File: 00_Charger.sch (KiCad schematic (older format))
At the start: 27 parts

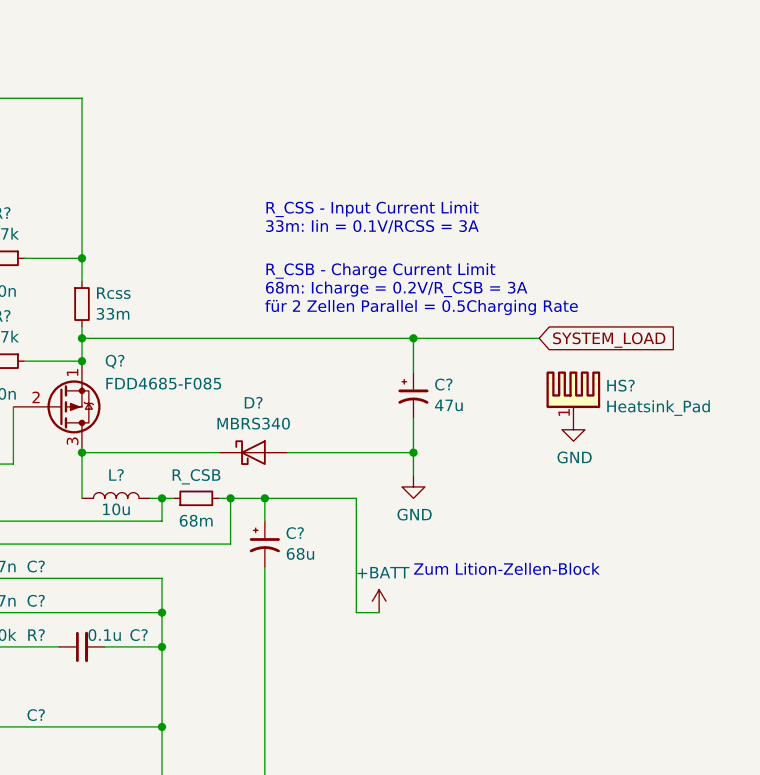
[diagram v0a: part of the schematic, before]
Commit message: BMS fertig, Charger fertig, Amplifier fertig. TODO: Charge vs Discharge LiPo wie machen sachen
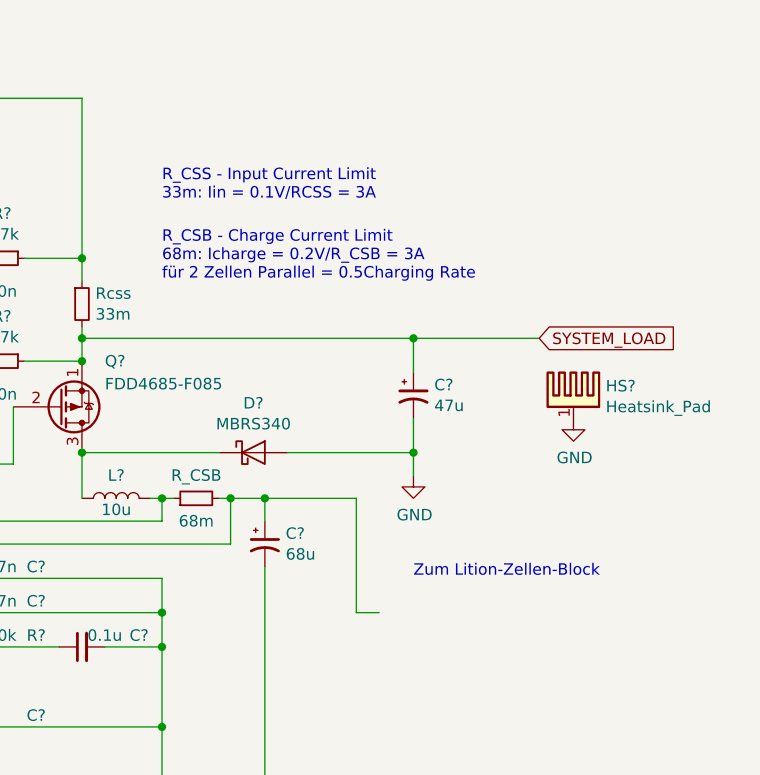
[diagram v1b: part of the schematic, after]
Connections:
- net labels removed: +BATT
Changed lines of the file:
@@
-$EndComp
-$Comp
-L Device:CP1_Small C?
-U 1 1 5E75D16E
-P 8050 3400
-F 0 "C?" H 8141 3446 50  0000 L CNN
-F 1 "47u" H 8141 3355 50  0000 L CNN
-F 2 "" H 8050 3400 50  0001 C CNN
-F 3 "~" H 8050 3400 50  0001 C CNN
-	1    8050 3400
-	1    0    0    -1
 $EndComp
 $Comp
@@
 Connection ~ 6600 2800
 Wire Wire Line
-	6600 3100 6600 3150
-Wire Wire Line
 	6600 3250 6350 3250
 Wire Wire Line
@@
 	7400 3850 7400 3950
 Connection ~ 7250 3850
-Wire Wire Line
-	7400 3850 7800 3850
-Wire Wire Line
-	7800 3850 7800 4350
 Connection ~ 7400 3850
 $Comp
@@
 	1    0    0    -1
 $EndComp
-Wire Wire Line
-	8050 3150 8050 3300
 $Comp
 L Device:D_Schottky D?
@@
 Wire Wire Line
 	6600 3650 7200 3650
-Wire Wire Line
-	6600 3150 8050 3150
-Connection ~ 6600 3150
-Wire Wire Line
-	6600 3150 6600 3250
 Connection ~ 6600 3250
 Wire Wire Line
@@
 Wire Wire Line
 	6950 3850 6950 3950
-Wire Wire Line
-	8050 3500 8050 3650
-Wire Wire Line
-	7500 3650 8050 3650
-Connection ~ 8050 3650
-Wire Wire Line
-	8050 3650 8050 3750
-Text GLabel 8600 3150 2    50   Input ~ 0
-SYSTEM_LOAD
-Wire Wire Line
-	8600 3150 8050 3150
-Connection ~ 8050 3150
 $Comp
 L Device:Q_NMOS_DGS Q?
@@
 Wire Wire Line
 	2700 3850 2950 3850
-Text Notes 7400 3050 0    50   ~ 0
+Text Notes 6950 2900 0    50   ~ 0
 R_CSB - Charge Current Limit\n68m: Icharge = 0.2V/R_CSB = 3A\nfür 2 Zellen Parallel = 0.5Charging Rate\n
 Text Notes 4000 5600 0    50   ~ 0
@@
 Text Notes 4900 1650 0    50   ~ 0
 T Version des IC für 4 Li-Ion Zellen
-$Comp
-L power:+BATT #PWR?
-U 1 1 5E811BF9
-P 7900 4350
-F 0 "#PWR?" H 7900 4200 50  0001 C CNN
-F 1 "+BATT" H 7915 4523 50  0000 C CNN
-F 2 "" H 7900 4350 50  0001 C CNN
-F 3 "" H 7900 4350 50  0001 C CNN
-	1    7900 4350
-	1    0    0    -1
-$EndComp
-Wire Wire Line
-	7900 4350 7800 4350
-Text Notes 7400 2700 0    50   ~ 0
+Text Notes 6950 2550 0    50   ~ 0
 R_CSS - Input Current Limit\n33m: Iin = 0.1V/RCSS = 3A
 $Comp
@@
 	1    0    0    -1
 $EndComp
+Wire Wire Line
+	7400 3850 7800 3850
+Wire Wire Line
+	7800 3850 7800 4350
+Wire Wire Line
+	7900 4350 7800 4350
+Wire Wire Line
+	8050 3650 8050 3750
+Wire Wire Line
+	7500 3650 8050 3650
+Connection ~ 8050 3650
+Wire Wire Line
+	8050 3500 8050 3650
+Wire Wire Line
+	8050 3150 8050 3300
+Wire Wire Line
+	8600 3150 8050 3150
+Connection ~ 8050 3150
+Wire Wire Line
+	6600 3150 6600 3250
+Wire Wire Line
+	6600 3100 6600 3150
+Connection ~ 6600 3150
+Wire Wire Line
+	6600 3150 8050 3150
+$Comp
+L Device:CP1_Small C?
+U 1 1 5E75D16E
+P 8050 3400
+F 0 "C?" H 8141 3446 50  0000 L CNN
+F 1 "47u" H 8141 3355 50  0000 L CNN
+F 2 "" H 8050 3400 50  0001 C CNN
+F 3 "~" H 8050 3400 50  0001 C CNN
+	1    8050 3400
+	1    0    0    -1
+$EndComp
+Text GLabel 8600 3150 2    50   Input ~ 0
+SYSTEM_LOAD
 $EndSCHEMATC

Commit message: 3v3 über LDO von BMS enablen. Bluetooth hinzugefügt
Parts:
- added J401: Jack-DC, symbol Connector:Jack-DC
- gave numbers to parts that had none: 25
- renumbered R_CSB to R_CSB401, Rcss to Rcss401
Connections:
- net labels added: DC_20V_POWER_SUPPLY, GNDPWR, PACK+
- net labels removed: VCC
- wire segments 81 -> 82
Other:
- note added: "GND über Shunt verbinden"
- note added: "Spannung 20V in Ladekabel"

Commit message: Schaltplan fertig. Fertig für review
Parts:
- removed Q401: NMOS, symbol Device:Q_NMOS_DGS
- added C?: 1000uF, symbol Device:C_Small
- added L?: 25mH, symbol Device:L_Small
- added Q?: NTK3043N, symbol Device:Q_NMOS_GSD
- added R?: 10k, symbol Device:R_Small
- added R?: 100K, symbol Device:R_Small
- added R? (x7): 1K, symbol Device:R_Small
- added R?: 10K, symbol Device:R_Small
- added R?: 1M, symbol Device:R_Small
- added U?: PC827, Package_DIP:DIP-8_W7.62mm, symbol Isolator:PC827
- L401: value 10u -> 10uH
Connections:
- net CHARGER_DISABLE: now also R?.1
- net CHARGER_IOUT: now also R?.1, R?.2; no longer U401.7 (IOUT)
- net DC_20V_POWER_SUPPLY: now also R?.1, R?.2
- net GND: now also Q?.2 (S), R?.1, R?.1, R?.2, U?.2, U?.7
- net GNDPWR: now also C?.2
- net at C402.1, C403.2, R405.1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: now also C?.1, L?.2; no longer D401.1 (K)
- net at R401.2, U401.6 (ICHG/EN): now also Q?.3 (D)
- new net: D401.1 (K), L?.1
- new net: Q?.1 (G), R?.1, R?.2
- new net: R?.2, U?.1
- new net: R?.1, R?.2 (x4)
- new net +3V3: R?.1
- new net CHARGER_PLUGGED: R?.2, U?.8
- new net IOUT: R?.2, U401.7 (IOUT)
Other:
- note added: "3,06V @ 3A Chargecurrent"
- note added: "4,08V @ 3A Chargecurrent"
- note added: "I=1mA"
- note added: "IOUT=20(R_SCB*I_CHG) = \n20*0,068*3A= 4,08V"
- note added: "LC-Tiefpass\n32Hz Grenzfrequenz"
- moved on the sheet: C401, C402, C403, C404, C405, C406, C407, C408, C409, C410, C411, C412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

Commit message: Footprintzuordnung angefangen
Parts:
- C401, C402, C403, C404, C405, C406, C407, C408, C409, C410: footprint (none) -> Capacitor_SMD:C_0603_1608Metric_Pad1.05x0.95mm_HandSolder
- C411, C412: footprint (none) -> Capacitor_SMD:CP_Elec_5x5.4
- C413: renamed from C?; footprint (none) -> Capacitor_SMD:CP_Elec_16x17.5
- gave numbers to parts that had none: 14
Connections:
- net POWER_SUPPLY: now reaches C402.1, C403.2, C413.1, L402.2, R405.1, Rcss401.1, U401.15 (DCIN)
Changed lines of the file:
@@
 F 0 "C408" V 7400 4100 50  0000 C CNN
 F 1 "47n" V 7400 4300 50  0000 C CNN
-F 2 "" H 7350 4450 50  0001 C CNN
+F 2 "Capacitor_SMD:C_0603_1608Metric_Pad1.05x0.95mm_HandSolder" H 7350 4450 50  0001 C CNN
 F 3 "~" H 7350 4450 50  0001 C CNN
 	1    7350 4450
@@
 F 0 "C401" H 4958 4004 50  0000 R CNN
 F 1 "1u" H 4958 4095 50  0000 R CNN
-F 2 "" H 5050 4050 50  0001 C CNN
+F 2 "Capacitor_SMD:C_0603_1608Metric_Pad1.05x0.95mm_HandSolder" H 5050 4050 50  0001 C CNN
 F 3 "~" H 5050 4050 50  0001 C CNN
 	1    5050 4050
@@
 F 0 "C409" V 7400 4650 50  0000 C CNN
 F 1 "1n" V 7400 4850 50  0000 C CNN
-F 2 "" H 7350 4950 50  0001 C CNN
+F 2 "Capacitor_SMD:C_0603_1608Metric_Pad1.05x0.95mm_HandSolder" H 7350 4950 50  0001 C CNN
 F 3 "~" H 7350 4950 50  0001 C CNN
 	1    7350 4950
@@
 F 0 "C402" V 5221 3100 50  0000 C CNN
 F 1 "220n" V 5312 3100 50  0000 C CNN
-F 2 "" H 5450 3100 50  0001 C CNN
+F 2 "Capacitor_SMD:C_0603_1608Metric_Pad1.05x0.95mm_HandSolder" H 5450 3100 50  0001 C CNN
 F 3 "~" H 5450 3100 50  0001 C CNN
 	1    5450 3100
@@
 F 0 "C407" V 7400 3950 50  0000 C CNN
 F 1 "47n" V 7400 4150 50  0000 C CNN
-F 2 "" H 7350 4300 50  0001 C CNN
+F 2 "Capacitor_SMD:C_0603_1608Metric_Pad1.05x0.95mm_HandSolder" H 7350 4300 50  0001 C CNN
 F 3 "~" H 7350 4300 50  0001 C CNN
 	1    7350 4300
@@
 F 0 "C410" V 7950 4350 50  0000 C CNN
 F 1 "0.1u" V 7900 4500 50  0000 C CNN
-F 2 "" H 7850 4600 50  0001 C CNN
+F 2 "Capacitor_SMD:C_0603_1608Metric_Pad1.05x0.95mm_HandSolder" H 7850 4600 50  0001 C CNN
 F 3 "~" H 7850 4600 50  0001 C CNN
 	1    7850 4600
@@
 F 0 "C403" V 5471 2900 50  0000 C CNN
 F 1 "220n" V 5562 2900 50  0000 C CNN
-F 2 "" H 5700 2900 50  0001 C CNN
+F 2 "Capacitor_SMD:C_0603_1608Metric_Pad1.05x0.95mm_HandSolder" H 5700 2900 50  0001 C CNN
 F 3 "~" H 5700 2900 50  0001 C CNN
 	1    5700 2900
@@
 F 0 "C404" V 6371 2450 50  0000 C CNN
 F 1 "2.2u" V 6462 2450 50  0000 C CNN
-F 2 "" H 6600 2450 50  0001 C CNN
+F 2 "Capacitor_SMD:C_0603_1608Metric_Pad1.05x0.95mm_HandSolder" H 6600 2450 50  0001 C CNN
 F 3 "~" H 6600 2450 50  0001 C CNN
 	1    6600 2450
@@
 F 0 "C405" H 7208 2954 50  0000 R CNN
 F 1 "220n" H 7208 3045 50  0000 R CNN
-F 2 "" H 7300 3000 50  0001 C CNN
+F 2 "Capacitor_SMD:C_0603_1608Metric_Pad1.05x0.95mm_HandSolder" H 7300 3000 50  0001 C CNN
 F 3 "~" H 7300 3000 50  0001 C CNN
 	1    7300 3000
@@
 F 0 "C406" H 7208 3404 50  0000 R CNN
 F 1 "220n" H 7208 3495 50  0000 R CNN
-F 2 "" H 7300 3450 50  0001 C CNN
+F 2 "Capacitor_SMD:C_0603_1608Metric_Pad1.05x0.95mm_HandSolder" H 7300 3450 50  0001 C CNN
 F 3 "~" H 7300 3450 50  0001 C CNN
 	1    7300 3450
@@
 	7850 2900 7600 2900
 Wire Wire Line
-	5550 2200 7850 2200
+	5550 2200 7450 2200
 Wire Wire Line
 	7850 2200 7850 2900
@@
 F 0 "C411" H 8741 4196 50  0000 L CNN
 F 1 "68u" H 8741 4105 50  0000 L CNN
-F 2 "" H 8650 4150 50  0001 C CNN
+F 2 "Capacitor_SMD:CP_Elec_5x5.4" H 8650 4150 50  0001 C CNN
 F 3 "~" H 8650 4150 50  0001 C CNN
 	1    8650 4150
@@
 	9300 3250 9300 3400
 Wire Wire Line
-	9850 3250 9300 3250
+	9850 3250 9600 3250
 Connection ~ 9300 3250
 Wire Wire Line
@@
 F 0 "C412" H 9391 3546 50  0000 L CNN
 F 1 "47u" H 9391 3455 50  0000 L CNN
-F 2 "" H 9300 3500 50  0001 C CNN
+F 2 "Capacitor_SMD:CP_Elec_5x5.4" H 9300 3500 50  0001 C CNN
 F 3 "~" H 9300 3500 50  0001 C CNN
 	1    9300 3500
@@
 DC_20V_POWER_SUPPLY
 $Comp
-L Device:Q_NMOS_GSD Q?
+L Device:Q_NMOS_GSD Q401
 U 1 1 5ECEE149
 P 4400 3950
-F 0 "Q?" H 4606 3996 50  0000 L CNN
+F 0 "Q401" H 4606 3996 50  0000 L CNN
 F 1 "NTK3043N" H 4606 3905 50  0000 L CNN
 F 2 "" H 4600 4050 50  0001 C CNN
@@
 $EndComp
 $Comp
-L Device:R_Small R?
+L Device:R_Small R415
 U 1 1 5ECEF6C1
 P 3850 3950
-F 0 "R?" V 3750 4000 50  0000 R CNN
+F 0 "R415" V 3750 4000 50  0000 R CNN
 F 1 "10k" V 3650 4000 50  0000 R CNN
 F 2 "" H 3850 3950 50  0001 C CNN
@@
 	3750 3950 3600 3950
 $Comp
-L Device:R_Small R?
+L Device:R_Small R417
 U 1 1 5EE5F4E2
 P 4100 4350
-F 0 "R?" H 4159 4396 50  0000 L CNN
+F 0 "R417" H 4159 4396 50  0000 L CNN
 F 1 "100K" H 4159 4305 50  0000 L CNN
 F 2 "" H 4100 4350 50  0001 C CNN
@@
 	4100 3950 4200 3950
 $Comp
-L power:GND #PWR?
+L power:GND #PWR0407
 U 1 1 5EE6150A
 P 4100 5200
-F 0 "#PWR?" H 4100 4950 50  0001 C CNN
+F 0 "#PWR0407" H 4100 4950 50  0001 C CNN
 F 1 "GND" H 4105 5027 50  0000 C CNN
 F 2 "" H 4100 5200 50  0001 C CNN
@@
 	4100 5200 4100 4450
 $Comp
-L Device:L_Small L?
+L Device:L_Small L402
 U 1 1 5EE6657B
 P 5000 2200
-F 0 "L?" V 5185 2200 50  0000 C CNN
+F 0 "L402" V 5185 2200 50  0000 C CNN
 F 1 "25mH" V 5094 2200 50  0000 C CNN
 F 2 "" H 5000 2200 50  0001 C CNN
@@
 Connection ~ 5550 2200
 $Comp
-L Device:C_Small C?
+L Device:C_Small C413
 U 1 1 5EE6A868
 P 5200 2400
-F 0 "C?" H 4850 2450 50  0000 L CNN
+F 0 "C413" H 4850 2450 50  0000 L CNN
 F 1 "1000uF" H 4850 2300 50  0000 L CNN
-F 2 "" H 5200 2400 50  0001 C CNN
+F 2 "Capacitor_SMD:CP_Elec_16x17.5" H 5200 2400 50  0001 C CNN
 F 3 "~" H 5200 2400 50  0001 C CNN
 	1    5200 2400
@@
 	5200 2200 5100 2200
 $Comp
-L power:GNDPWR #PWR?
+L power:GNDPWR #PWR0408
 U 1 1 5EE6CAF0
 P 5200 2500
-F 0 "#PWR?" H 5200 2300 50  0001 C CNN
+F 0 "#PWR0408" H 5200 2300 50  0001 C CNN
 F 1 "GNDPWR" H 5204 2346 50  0000 C CNN
 F 2 "" H 5200 2450 50  0001 C CNN
@@
 LC-Tiefpass\n32Hz Grenzfrequenz
 $Comp
-L Isolator:PC827 U?
+L Isolator:PC827 U402
 U 1 1 5EE6E88A
 P 3650 2900
-F 0 "U?" H 3650 3225 50  0000 C CNN
+F 0 "U402" H 3650 3225 50  0000 C CNN
 F 1 "PC827" H 3650 3134 50  0000 C CNN
 F 2 "Package_DIP:DIP-8_W7.62mm" H 3450 2700 50  0001 L CIN
@@
 	3350 2800 3150 2800
 $Comp
-L power:GND #PWR?
+L power:GND #PWR0404
 U 1 1 5EE80AA2
 P 3250 3100
-F 0 "#PWR?" H 3250 2850 50  0001 C CNN
+F 0 "#PWR0404" H 3250 2850 50  0001 C CNN
 F 1 "GND" H 3255 2927 50  0000 C CNN
 F 2 "" H 3250 3100 50  0001 C CNN
@@
 	2350 2200 2700 2200
 $Comp
-L Device:R_Small R?
+L Device:R_Small R412
 U 1 1 5EE96D0F
 P 3150 2300
-F 0 "R?" H 3209 2346 50  0000 L CNN
+F 0 "R412" H 3209 2346 50  0000 L CNN
 F 1 "1K" H 3209 2255 50  0000 L CNN
 F 2 "" H 3150 2300 50  0001 C CNN
@@
 	3150 2200 4450 2200
 $Comp
-L Device:R_Small R?
+L Device:R_Small R413
 U 1 1 5EE96E03
 P 3150 2500
-F 0 "R?" H 3209 2546 50  0000 L CNN
+F 0 "R413" H 3209 2546 50  0000 L CNN
 F 1 "1K" H 3209 2455 50  0000 L CNN
 F 2 "" H 3150 2500 50  0001 C CNN
@@
 $EndComp
 $Comp
-L Device:R_Small R?
+L Device:R_Small R414
 U 1 1 5EE96E5D
 P 3150 2700
-F 0 "R?" H 3209 2746 50  0000 L CNN
+F 0 "R414" H 3209 2746 50  0000 L CNN
 F 1 "1K" H 3209 2655 50  0000 L CNN
 F 2 "" H 3150 2700 50  0001 C CNN
@@
 $EndComp
 $Comp
-L power:+3V3 #PWR?
+L power:+3V3 #PWR0406
 U 1 1 5EE99664
 P 4050 2600
-F 0 "#PWR?" H 4050 2450 50  0001 C CNN
+F 0 "#PWR0406" H 4050 2450 50  0001 C CNN
 F 1 "+3V3" H 4065 2773 50  0000 C CNN
 F 2 "" H 4050 2600 50  0001 C CNN
@@
 $EndComp
 $Comp
-L Device:R_Small R?
+L Device:R_Small R416
 U 1 1 5EE996BE
 P 4050 2700
-F 0 "R?" H 4109 2746 50  0000 L CNN
+F 0 "R416" H 4109 2746 50  0000 L CNN
 F 1 "10K" H 4109 2655 50  0000 L CNN
 F 2 "" H 4050 2700 50  0001 C CNN
@@
 	4050 2800 3950 2800
 $Comp
-L power:GND #PWR?
+L power:GND #PWR0405
 U 1 1 5EE9BFF0
 P 4000 3100
-F 0 "#PWR?" H 4000 2850 50  0001 C CNN
+F 0 "#PWR0405" H 4000 2850 50  0001 C CNN
 F 1 "GND" H 4005 2927 50  0000 C CNN
 F 2 "" H 4000 3100 50  0001 C CNN
@@
 Connection ~ 4050 2800
 $Comp
-L Device:R_Small R?
+L Device:R_Small R411
 U 1 1 5EEA2289
 P 2700 2700
-F 0 "R?" H 2641 2654 50  0000 R CNN
+F 0 "R411" H 2641 2654 50  0000 R CNN
 F 1 "1M" H 2641 2745 50  0000 R CNN
 F 2 "" H 2700 2700 50  0001 C CNN
@@
 	2700 2200 3150 2200
 $Comp
-L power:GND #PWR?
+L power:GND #PWR0403
 U 1 1 5EEA50EF
 P 2700 3100
-F 0 "#PWR?" H 2700 2850 50  0001 C CNN
+F 0 "#PWR0403" H 2700 2850 50  0001 C CNN
 F 1 "GND" H 2705 2927 50  0000 C CNN
 F 2 "" H 2700 3100 50  0001 C CNN
@@
 IOUT=20(R_SCB*I_CHG) = \n20*0,068*3A= 4,08V
 $Comp
-L Device:R_Small R?
+L Device:R_Small R407
 U 1 1 5EF7027C
 P 2300 3750
-F 0 "R?" H 2241 3704 50  0000 R CNN
+F 0 "R407" H 2241 3704 50  0000 R CNN
 F 1 "1K" H 2241 3795 50  0000 R CNN
 F 2 "" H 2300 3750 50  0001 C CNN
@@
 	2300 3550 2200 3550
 $Comp
-L Device:R_Small R?
+L Device:R_Small R408
 U 1 1 5EF79B9A
 P 2300 4100
-F 0 "R?" H 2241 4054 50  0000 R CNN
+F 0 "R408" H 2241 4054 50  0000 R CNN
 F 1 "1K" H 2241 4145 50  0000 R CNN
 F 2 "" H 2300 4100 50  0001 C CNN
@@
 $EndComp
 $Comp
-L Device:R_Small R?
+L Device:R_Small R409
 U 1 1 5EF79C18
 P 2300 4300
-F 0 "R?" H 2241 4254 50  0000 R CNN
+F 0 "R409" H 2241 4254 50  0000 R CNN
 F 1 "1K" H 2241 4345 50  0000 R CNN
 F 2 "" H 2300 4300 50  0001 C CNN
@@
 $EndComp
 $Comp
-L Device:R_Small R?
+L Device:R_Small R410
 U 1 1 5EF79C92
 P 2300 4500
-F 0 "R?" H 2241 4454 50  0000 R CNN
+F 0 "R410" H 2241 4454 50  0000 R CNN
 F 1 "1K" H 2241 4545 50  0000 R CNN
 F 2 "" H 2300 4500 50  0001 C CNN
@@
 $EndComp
 $Comp
-L power:GND #PWR?
+L power:GND #PWR0402
 U 1 1 5EF79D24
 P 2300 4600
-F 0 "#PWR?" H 2300 4350 50  0001 C CNN
+F 0 "#PWR0402" H 2300 4350 50  0001 C CNN
 F 1 "GND" H 2305 4427 50  0000 C CNN
 F 2 "" H 2300 4600 50  0001 C CNN
@@
 Text Notes 2300 3600 0    50   ~ 0
 I=1mA
+$Comp
+L power:PWR_FLAG #FLG0105
+U 1 1 5EB86DAB
+P 9600 3250
+F 0 "#FLG0105" H 9600 3325 50  0001 C CNN
+F 1 "PWR_FLAG" H 9600 3424 50  0000 C CNN
+F 2 "" H 9600 3250 50  0001 C CNN
+F 3 "~" H 9600 3250 50  0001 C CNN
+	1    9600 3250
+	1    0    0    -1
+$EndComp
+Connection ~ 9600 3250
+Wire Wire Line
+	9600 3250 9300 3250
+Text Label 7850 2200 0    50   ~ 0
+POWER_SUPPLY
+$Comp
+L power:PWR_FLAG #FLG0106
+U 1 1 5EB87FDB
+P 7450 2200
+F 0 "#FLG0106" H 7450 2275 50  0001 C CNN
+F 1 "PWR_FLAG" H 7450 2374 50  0000 C CNN
+F 2 "" H 7450 2200 50  0001 C CNN
+F 3 "~" H 7450 2200 50  0001 C CNN
+	1    7450 2200
+	1    0    0    -1
+$EndComp
+Connection ~ 7450 2200
+Wire Wire Line
+	7450 2200 7850 2200
 $EndSCHEMATC

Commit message: fast alle footprints herausgesucht. Spulen typen rausgesucht: Bourns spulen
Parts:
- removed C413: 1000uF, Capacitor_SMD:CP_Elec_16x17.5, symbol Device:C_Small
- removed L402: 25mH, symbol Device:L_Small
- added HS402, HS403: Heatsink_Pad, Heatsink:Heatsink_AAVID_573300D00010G_TO-263, symbol Mechanical:Heatsink_Pad
- D401, D402: value MBRS340 -> STPS2045C; footprint (none) -> Package_TO_SOT_SMD:TO-263-2
- HS401: footprint (none) -> Heatsink:Heatsink_AAVID_573300D00010G_TO-263
- L401: value 10uH -> 10uH PQ2614BLA-100K; footprint (none) -> Inductor_SMD:PQ2617BHA-330K
- Q401: footprint (none) -> Package_TO_SOT_SMD:SOT-723
- Q402: footprint (none) -> Package_TO_SOT_SMD:TO-263-2
- R401, R402, R403, R404, R405, R406, R407, R408, R409, R410, R411, R412, R413, R414, R415, R416, R417: footprint (none) -> Resistor_SMD:R_0603_1608Metric_Pad1.05x0.95mm_HandSolder
- R_CSB401, Rcss401: footprint (none) -> Resistor_SMD:R_1206_3216Metric_Pad1.42x1.75mm_HandSolder
- U402: footprint Package_DIP:DIP-8_W7.62mm -> Package_DIP:DIP-8_W7.62mm_SMDSocket_SmallPads
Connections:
- net GND: no longer HS401.1
- net POWER_SUPPLY: now also D401.1 (K), HS401.1
- net at D402.1 (K), L401.1, Q402.3 (D): now also HS402.1, HS403.1
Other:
- note removed: "LC-Tiefpass\n32Hz Grenzfrequenz"

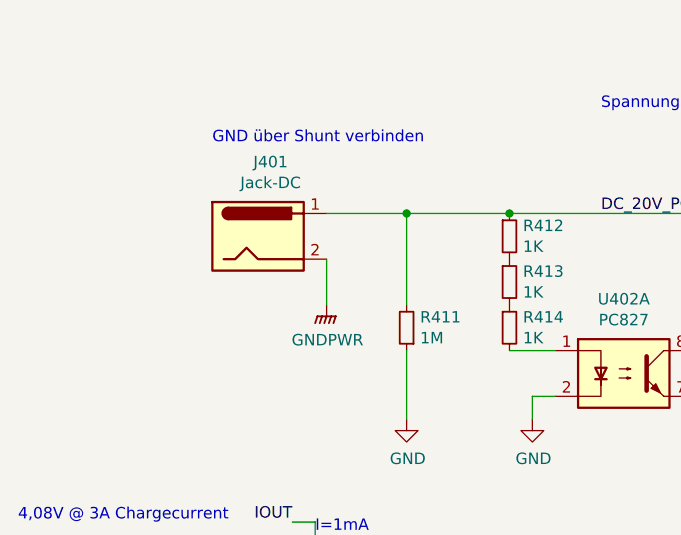
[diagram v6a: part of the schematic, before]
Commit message: Port Expander und Rotary Encoder hinzugefügt. TODO: Footprint Heatsink Amp
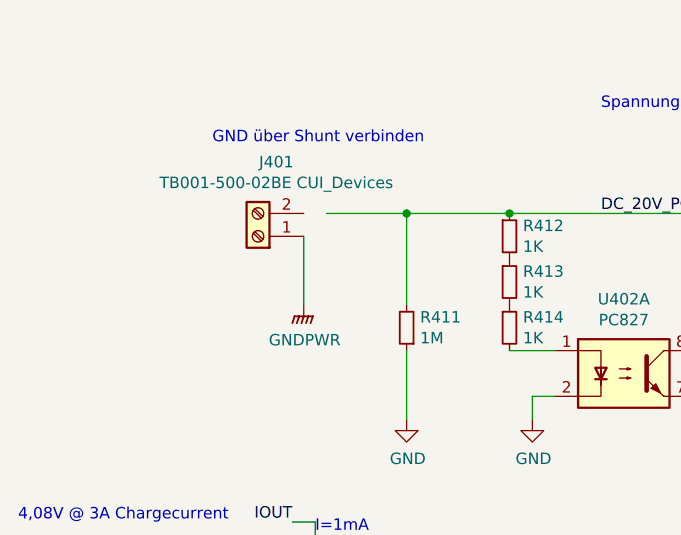
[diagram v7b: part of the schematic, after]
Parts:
- removed J401: Jack-DC, symbol Connector:Jack-DC
- added J401: TB001-500-02BE CUI_Devices, TerminalBlock_RND:TerminalBlock_RND_205-00045_1x02_P5.00mm_Horizontal, symbol Connector:Screw_Terminal_01x02
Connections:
- net GNDPWR: now also J401.1 (Pin_1)
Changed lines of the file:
@@
 $Descr A4 11693 8268
 encoding utf-8
-Sheet 4 7
+Sheet 4 8
 Title ""
 Date ""
@@
 Spannung 20V in Ladekabel
 $Comp
-L Connector:Jack-DC J401
-U 1 1 5E8B7937
-P 2050 2300
-F 0 "J401" H 2105 2625 50  0000 C CNN
-F 1 "Jack-DC" H 2105 2534 50  0000 C CNN
-F 2 "" H 2100 2260 50  0001 C CNN
-F 3 "~" H 2100 2260 50  0001 C CNN
-	1    2050 2300
-	1    0    0    -1
-$EndComp
-$Comp
 L power:GNDPWR #PWR0401
 U 1 1 5E8B9696
-P 2350 2600
-F 0 "#PWR0401" H 2350 2400 50  0001 C CNN
-F 1 "GNDPWR" H 2354 2446 50  0000 C CNN
-F 2 "" H 2350 2550 50  0001 C CNN
-F 3 "" H 2350 2550 50  0001 C CNN
-	1    2350 2600
-	1    0    0    -1
-$EndComp
-Wire Wire Line
-	2350 2600 2350 2400
+P 2250 2600
+F 0 "#PWR0401" H 2250 2400 50  0001 C CNN
+F 1 "GNDPWR" H 2254 2446 50  0000 C CNN
+F 2 "" H 2250 2550 50  0001 C CNN
+F 3 "" H 2250 2550 50  0001 C CNN
+	1    2250 2600
+	1    0    0    -1
+$EndComp
+Wire Wire Line
+	2250 2600 2250 2300
 Text Notes 1850 1900 0    50   ~ 0
 GND über Shunt verbinden
@@
 Wire Wire Line
 	4750 2200 5550 2200
+$Comp
+L Connector:Screw_Terminal_01x02 J401
+U 1 1 5F5663AE
+P 2050 2300
+F 0 "J401" H 1970 1975 50  0000 C CNN
+F 1 "TB001-500-02BE CUI_Devices" H 1970 2066 50  0000 C CNN
+F 2 "TerminalBlock_RND:TerminalBlock_RND_205-00045_1x02_P5.00mm_Horizontal" H 2050 2300 50  0001 C CNN
+F 3 "https://www.mouser.de/datasheet/2/670/tb001-500-1550615.pdf" H 2050 2300 50  0001 C CNN
+	1    2050 2300
+	-1   0    0    1
+$EndComp
 $EndSCHEMATC
